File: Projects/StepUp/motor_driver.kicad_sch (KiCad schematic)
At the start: 43 parts, among them J5 Conn_01x01_Pin, J6 Conn_01x01_Pin, J7 TBLH10-350-04BK, J8 Conn_01x01_Pin, J9 Conn_01x01_Pin, Q1 BSS84, Q2 2N7002, U4 TMC2300-LA

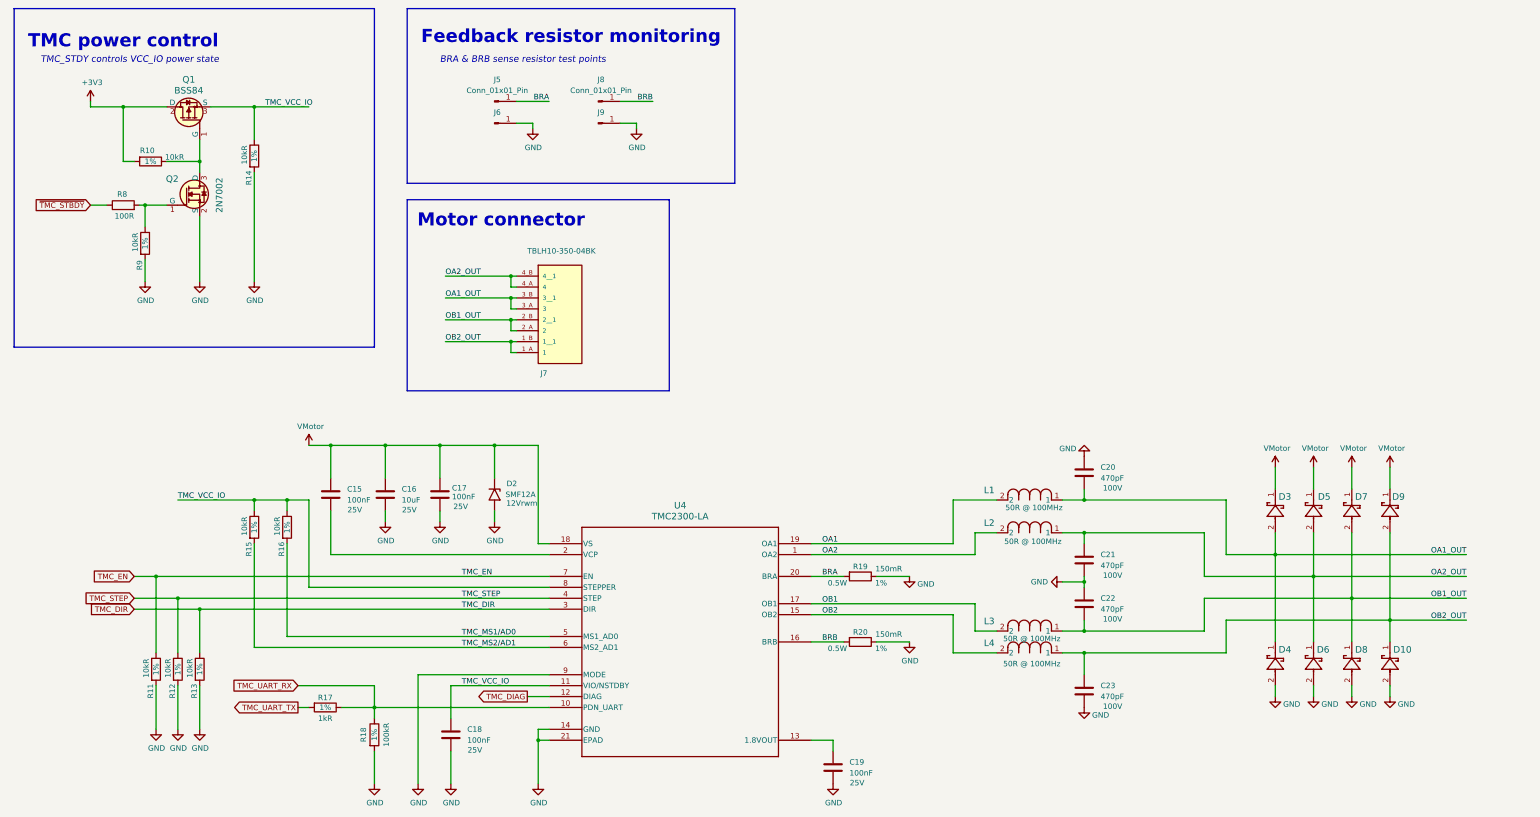
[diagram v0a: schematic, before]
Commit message: feat(layout): TMC & Boost layout begin
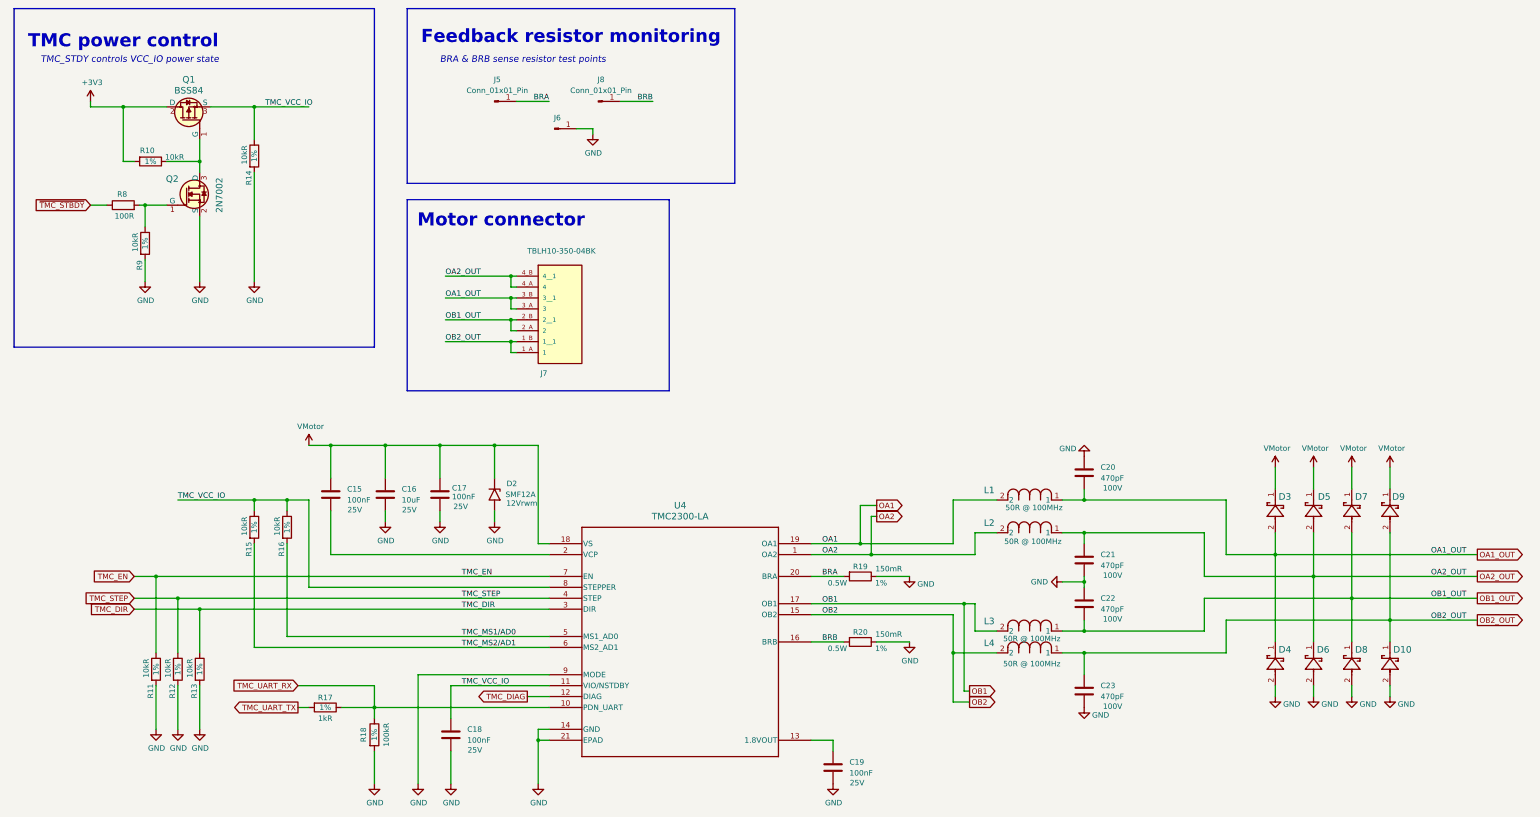
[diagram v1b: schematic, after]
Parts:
- removed J6: Conn_01x01_Pin, Connector_PinHeader_2.54mm:PinHeader_1x01_P2.54mm_Vertical, symbol Connector:Conn_01x01_Pin
- U4: footprint QFN20_3x3_TRI -> Ultra_librarian_footprints:QFN20_3x3_TRI
- renumbered J9 to J6
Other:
- moved on the sheet: J6

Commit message: feat(layout): DRC ongoing, layout nearly complete
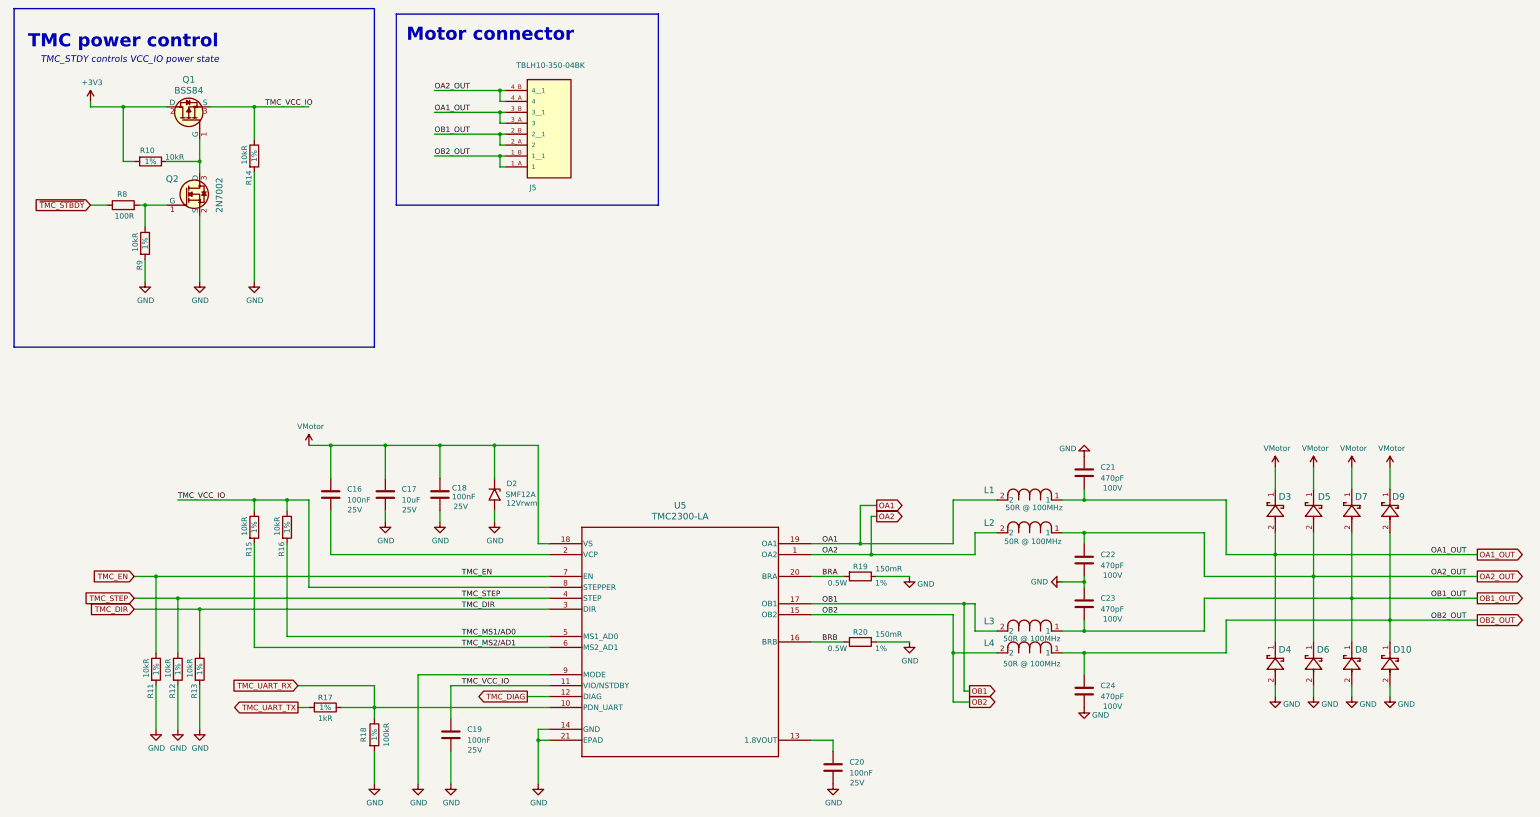
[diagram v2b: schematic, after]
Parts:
- removed J5, J6, J8: Conn_01x01_Pin, Connector_PinHeader_2.54mm:PinHeader_1x01_P2.54mm_Vertical, symbol Connector:Conn_01x01_Pin
- renumbered C15 to C16, C16 to C17, C17 to C18, C18 to C19, C19 to C20, C20 to C21, C21 to C22, C22 to C23, C23 to C24, J7 to J5, U4 to U5
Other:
- note removed: "BRA & BRB sense resistor test points"
- note removed: "Feedback resistor monitoring"
- moved on the sheet: J5

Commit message: feat(StepUp): Release v0.1
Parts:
- C16, C18, C19, C20, C21, C22, C23, C24: Package (none) -> 0402; Type (none) -> SMD
- C17: Package (none) -> 0603; Type (none) -> SMD
- D10, D3, D4, D5, D6, D7, D8, D9: MPN (none) -> B5819W-TP; Manufacturer (none) -> Micro Commercial Co; Type (none) -> SMD
- D2: MPN (none) -> SMF12A; Manufacturer (none) -> Vishay; Type (none) -> SMD
- J5: MPN (none) -> TBLH10-350-04BK; Manufacturer (none) -> CUI Devices; Type (none) -> thru-hole
- L1, L2, L3, L4: MPN (none) -> HI1206T500R-10; Manufacturer (none) -> Laird-Signal Integrity Products; Type (none) -> SMD
- Q1, Q2: Type (none) -> SMD
- R10: renamed from R8; Package (none) -> 0603; Tolerance (none) -> 1%; Type (none) -> SMD
- R11: renamed from R9; Package (none) -> 0603; Type (none) -> SMD
- R12: renamed from R10; Package (none) -> 0603; Type (none) -> SMD
- R13: renamed from R11; Package (none) -> 0603; Type (none) -> SMD
- R14: renamed from R12; Package (none) -> 0603; Type (none) -> SMD
- R15: renamed from R13; Package (none) -> 0603; Type (none) -> SMD
- R16: renamed from R14; Package (none) -> 0603; Type (none) -> SMD
- R17: renamed from R15; Package (none) -> 0603; Type (none) -> SMD
- R18: renamed from R16; Package (none) -> 0603; Type (none) -> SMD
- R19: renamed from R17; Package (none) -> 0603; Type (none) -> SMD
- R20: renamed from R18; Package (none) -> 0603; Type (none) -> SMD
- R21: renamed from R19; MPN (none) -> CRL1206-FW-R150ELF; Manufacturer (none) -> Bourns Inc.; Package (none) -> 1206; Type (none) -> SMD
- R22: renamed from R20; MPN (none) -> CRL1206-FW-R150ELF; Manufacturer (none) -> Bourns Inc.; Package (none) -> 1206; Type (none) -> SMD
- U5: MPN (none) -> TMC2300-LA; Manufacturer (none) -> Analog Devices Inc./Maxim Integrated; Type (none) -> SMD
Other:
- company: Samio -> SJFOM

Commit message: feat(outputs): Added STEP file & schematic output
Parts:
- U5: footprint Ultra_librarian_footprints:QFN20_3x3_TRI -> Ultra_librarian_footprints:QFN20_3x3_TRI-M
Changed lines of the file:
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@@
 			)
 		)
-		(property "Footprint" "Ultra_librarian_footprints:QFN20_3x3_TRI"
+		(property "Footprint" "Ultra_librarian_footprints:QFN20_3x3_TRI-M"
 			(at 144.78 148.59 0)
 			(effects

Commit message: feat(BoM): Updating PN's
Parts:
- C17: MPN (none) -> GRM188R61E106KA73D; Manufacturer (none) -> Murata Electronics
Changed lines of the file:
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@@
+			)
+		)
+		(property "MPN" "GRM188R61E106KA73D"
+			(at 106.68 135.89 0)
+			(effects
+				(font
+					(size 1.27 1.27)
+				)
+				(hide yes)
+			)
+		)
+		(property "Manufacturer" "Murata Electronics"
+			(at 106.68 135.89 0)
+			(effects
+				(font
+					(size 1.27 1.27)
+				)
+				(hide yes)
 			)
 		)

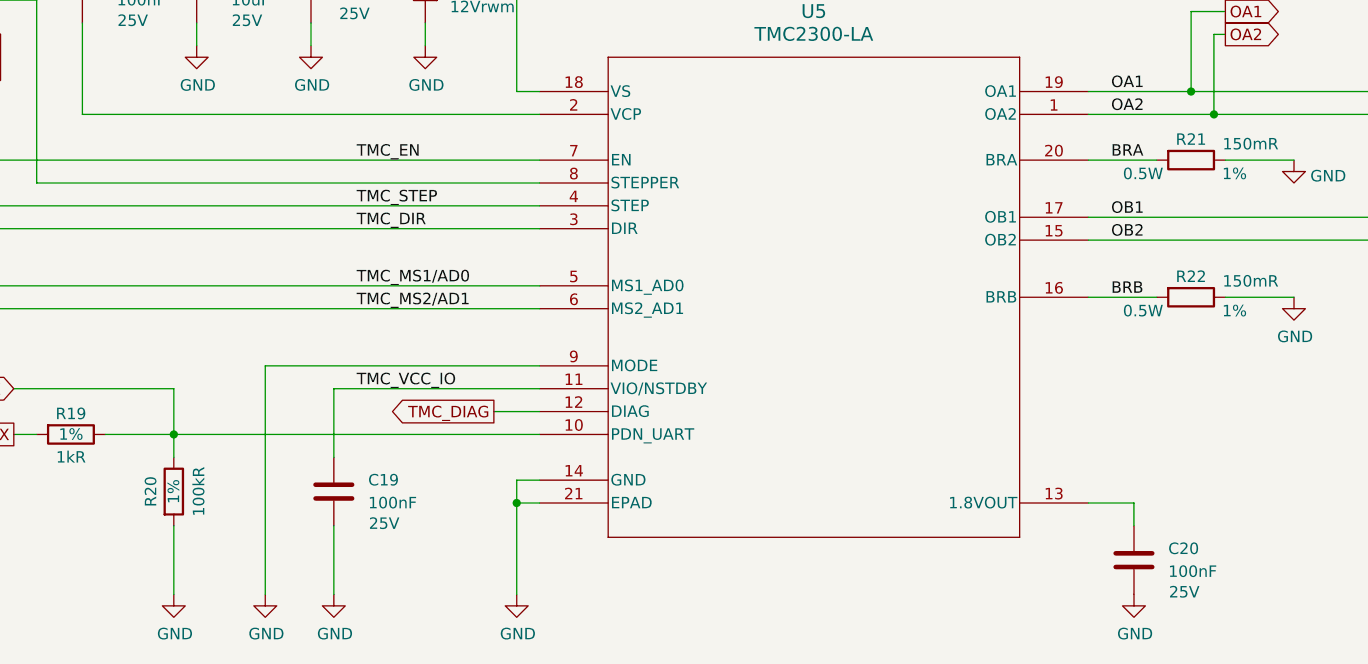
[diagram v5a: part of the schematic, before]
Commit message: chore(bom): Update from PCB BoM
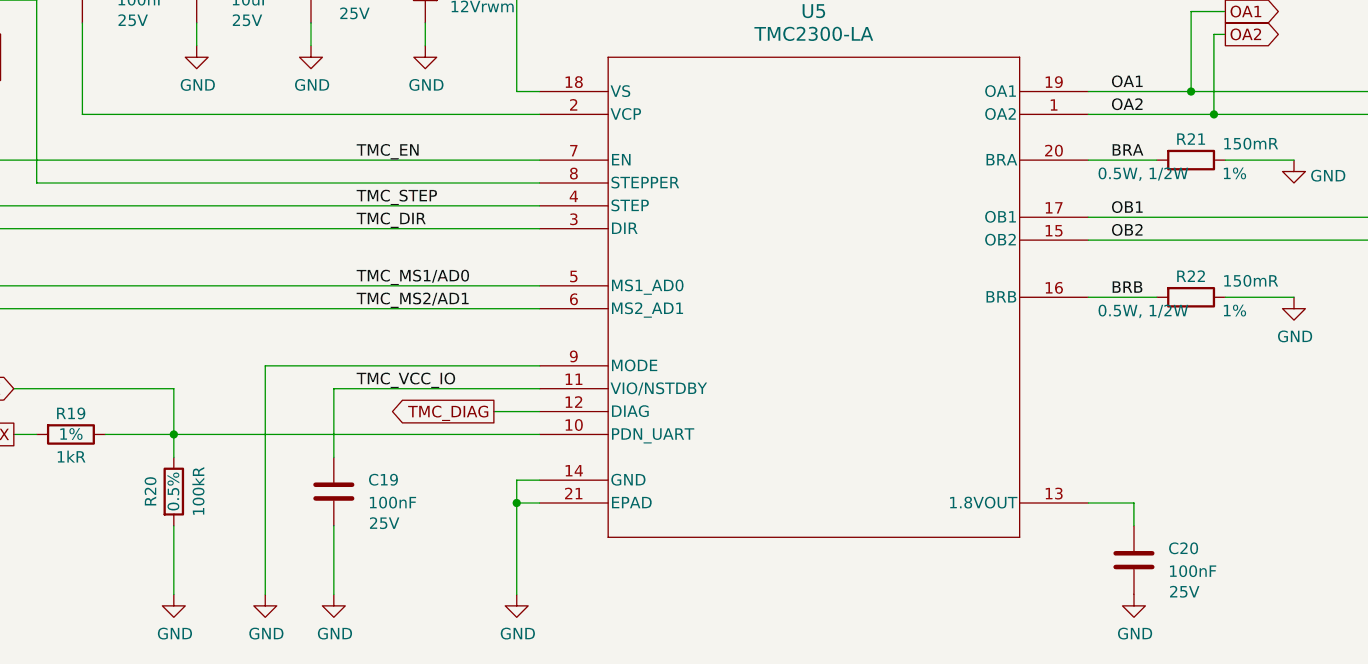
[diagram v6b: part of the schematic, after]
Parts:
- C16, C18, C19, C20: Dielectric (none) -> X7R; MPN (none) -> CC0402KRX7R8BB104; Manufacturer (none) -> YAGEO; Tolerance (none) -> 10%
- C17: Dielectric (none) -> X5R; Tolerance (none) -> 10%
- C21, C22, C23, C24: Dielectric (none) -> X7R; MPN (none) -> CC0402KRX7R0BB471; Manufacturer (none) -> YAGEO; Tolerance (none) -> 10%
- R10: MPN (none) -> RC0603FR-07100RL; Manufacturer (none) -> YAGEO; Power (none) -> 0.1W, 1/10W
- R11, R12, R13, R14, R15, R16, R17, R18: MPN (none) -> RC0603FR-0710KL; Manufacturer (none) -> YAGEO; Power (none) -> 0.1W, 1/10W
- R19: MPN (none) -> RC0603FR-071KL; Manufacturer (none) -> YAGEO; Power (none) -> 0.1W, 1/10W
- R20: MPN (none) -> RT0603DRE10100KL; Manufacturer (none) -> YAGEO; Power (none) -> 0.1W, 1/10W; Tolerance 1% -> 0.5%
- R21, R22: Power 0.5W -> 0.5W, 1/2W

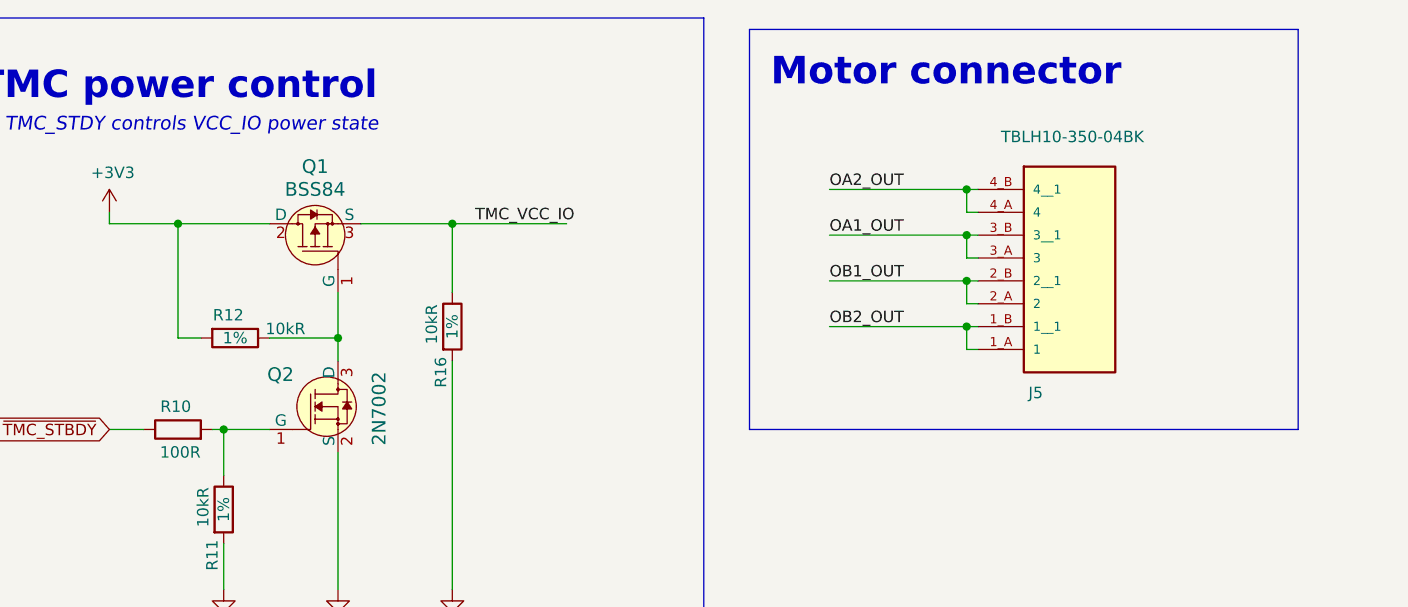
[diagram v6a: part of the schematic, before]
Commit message: feat(v0.2): Schematic updated, PCB layout start
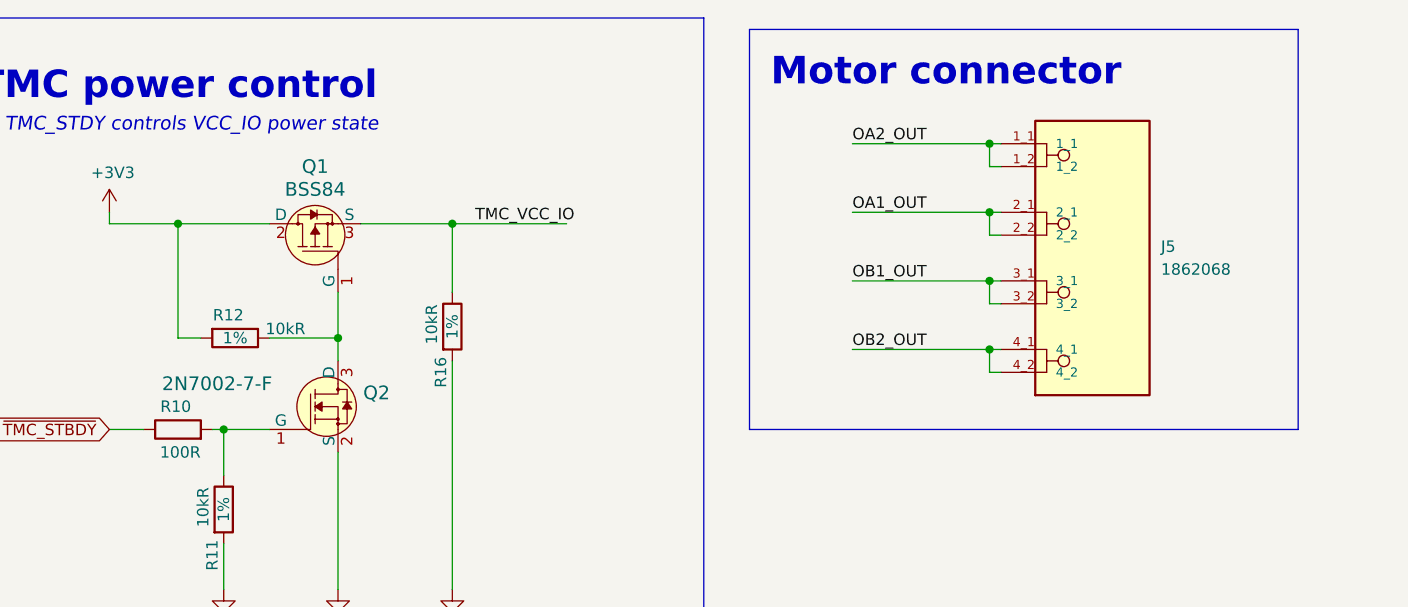
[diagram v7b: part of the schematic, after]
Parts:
- removed J5: TBLH10-350-04BK, Snapeda:CUI_TBLH10-350-04BK, symbol Snapeda:TBLH10-350-04BK
- removed Q2: 2N7002, digikey-footprints:SOT-23-3, symbol dk_Transistors-FETs-MOSFETs-Single:2N7002
- added J5: 1862068, Snapeda:1862068_PHOENIX_1862068, symbol Snapeda_kicad:1862068
- added Q2: 2N7002-7-F, digikey-footprints:SOT-23-3, symbol dk_Transistors-FETs-MOSFETs-Single:2N7002-7-F
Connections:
- net GND: now also Q2.2 (S)
- net OA1_OUT: now also J5.2_1, J5.2_2
- net OA2_OUT: now also J5.1_1, J5.1_2
- net OB1_OUT: now also J5.3_1, J5.3_2
- net OB2_OUT: now also J5.4_1, J5.4_2
- net at Q1.1 (G), R12.1: now also Q2.3 (D)
- net at R10.2, R11.1: now also Q2.1 (G)

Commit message: feat(v0.2): Rough layout begins
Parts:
- Q1: Description_1 (none) -> MOSFET P-CH 50V 130MA SOT-23; Digi-Key_PN (none) -> BSS84CT-ND
- renumbered C16 to C15, C17 to C16, C18 to C17, C19 to C18, C20 to C19, C21 to C20, C22 to C21, C23 to C22, C24 to C23, J5 to J3, R12 to R10, R13 to R11, R14 to R12, R15 to R13, R16 to R14, R17 to R15, R18 to R16, R19 to R17, R20 to R18, R21 to R19, R22 to R20, R10 to R8, R11 to R9, U5 to U4
